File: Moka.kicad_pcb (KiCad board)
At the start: 2 copper layers, 60 x 60 mm, 69 parts, among them J1 Conn_02x03_Odd_Even, J10 CONN_01X05, J2 GS2, J3 GS2, J4 GS2, J5 GS2, J6 GS2, J7 CONN_01X05, J8 CONN_01X05, J9 CONN_01X05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

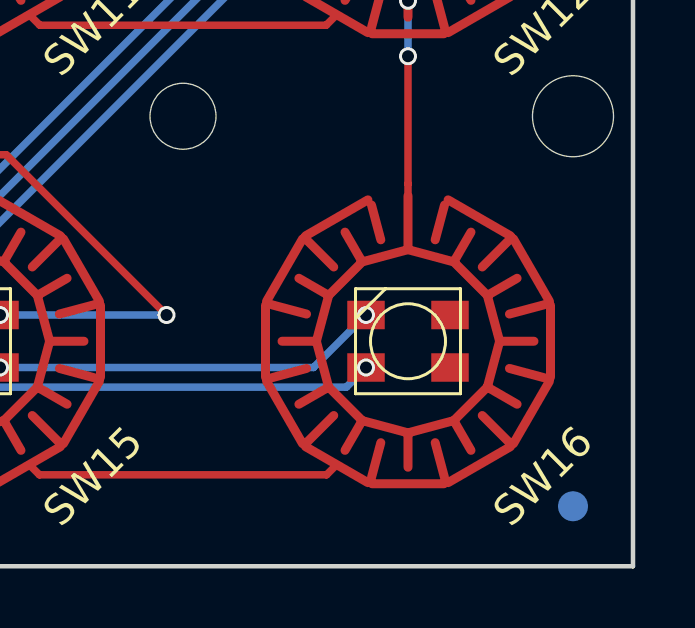
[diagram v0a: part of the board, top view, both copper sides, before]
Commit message: Fixed missing via on last led GND.
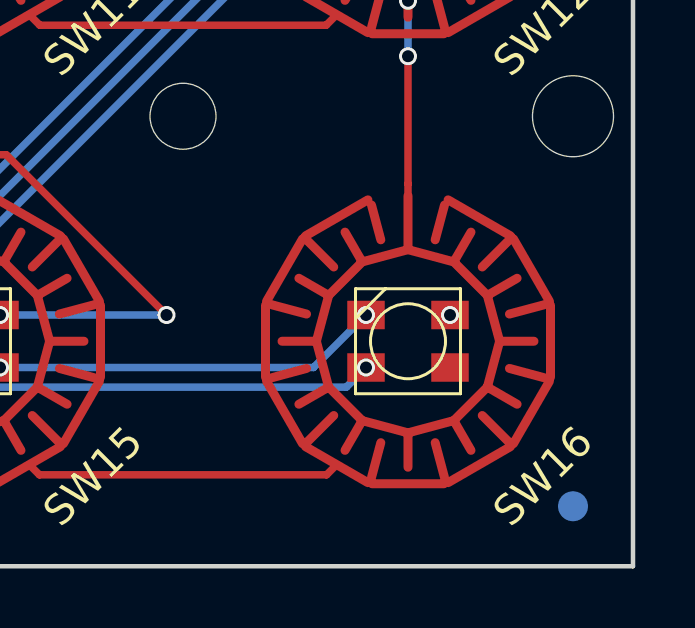
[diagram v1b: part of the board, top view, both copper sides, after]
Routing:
- net GND: vias 56 -> 57
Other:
- board text added: "v0.96"
- board text removed: "v0.95"
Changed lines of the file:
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@@
   (general
     (links 858)
-    (no_connects 721)
-    (area 134.924999 79.924999 195.075001 140.075001)
+    (no_connects 720)
+    (area 131.680952 74.578618 198.319048 142.885)
     (thickness 1.6)
     (drawings 39)
-    (tracks 1033)
+    (tracks 1034)
     (zones 0)
     (modules 69)
@@
     (pcbplotparams
       (layerselection 0x010fc_80000001)
-      (usegerberextensions true)
+      (usegerberextensions false)
       (excludeedgelayer true)
       (linewidth 0.100000)
@@
       (viasonmask false)
       (mode 1)
-      (useauxorigin true)
+      (useauxorigin false)
       (hpglpennumber 1)
       (hpglpenspeed 20)
@@
       (plotinvisibletext false)
       (padsonsilk false)
-      (subtractmaskfromsilk true)
-      (outputformat 1)
+      (subtractmaskfromsilk false)
+      (outputformat 4)
       (mirror false)
       (drillshape 0)
@@
     (effects (font (size 1.5 1.5) (thickness 0.3)) (justify mirror))
   )
-  (gr_text v0.95 (at 176.149 134.112) (layer B.SilkS)
+  (gr_text v0.96 (at 176.149 134.112) (layer B.SilkS)
     (effects (font (size 2.5 2.5) (thickness 0.3) italic) (justify mirror))
   )
@@
   (segment (start 137 112.54) (end 139.473 112.54) (width 0.25) (layer B.Cu) (net 1))
   (segment (start 139.473 112.54) (end 139.953 112.06) (width 0.25) (layer B.Cu) (net 1))
+  (via (at 188.9 131.625) (size 0.6) (drill 0.4) (layers F.Cu B.Cu) (net 2))
   (segment (start 148.081 116.632) (end 154.64 116.632) (width 0.25) (layer B.Cu) (net 2))
   (segment (start 154.64 116.632) (end 155.321 115.951) (width 0.25) (layer B.Cu) (net 2))
